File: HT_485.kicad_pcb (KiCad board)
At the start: 2 copper layers, 82 x 72.2 mm, 85 parts, among them J1 POWER, J2 485, J3 PT1000, J4 H/T Sensor, J5 PRG, Q1 BC817, Q2 BC817, Q3 BC817, Q4 BC817, U1 MAX14786EAUD+T, U2 TL082, U3 LM2576D2TR4-3.3G, U4 ESP32-S3-WROOM-1-N16R8, U5 CAT3200TDI-GT3, U6 L7815

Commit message: Rifatto schema 485. Master da rifare
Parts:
- removed C1: 4.7uF, Capacitor_SMD:C_0805_2012Metric
- removed C11, C12: 1uF, Capacitor_SMD:C_0805_2012Metric
- removed C13, C9: 10uF, Capacitor_SMD:C_0805_2012Metric
- removed C14, C15, C2, C20, C4, C8: 100nF, Capacitor_SMD:C_0805_2012Metric
- removed C16: 1nF, Capacitor_SMD:C_0805_2012Metric
- removed C17: 1uF/25V, Capacitor_SMD:C_0805_2012Metric
- removed C18, C19: 100uF/25V, Capacitor_SMD:CP_Elec_6.3x7.7
- removed C3: 1uF/16V, Capacitor_SMD:C_0805_2012Metric
- removed C5: 100uF / 50V, Capacitor_SMD:CP_Elec_8x10.5
- removed C6: 1nF/10V, Capacitor_SMD:C_0805_2012Metric
- removed C7: 1000uF/10V, Capacitor_SMD:CP_Elec_10x10.5
- removed D1: VS-30BQ060HM3/9AT, Diode_SMD:D_SMB-SMC_Universal_Handsoldering
- removed D10: STPS0520Z, Diode_SMD:D_SOD-123
- removed D2: 3.9V/1W, Diode_SMD:D_SMA
- removed D3: PWR, LED_SMD:LED_0805_2012Metric
- removed D4, D5, D6, D7, D8: 1N4148WS, Diode_SMD:D_SOD-323
- removed D9: BAV99, Package_TO_SOT_SMD:SOT-23
- removed J1: POWER, TerminalBlock_Phoenix:TerminalBlock_Phoenix_PT-1,5-2-3.5-H_1x02_P3.50mm_Horizontal
- removed J2: 485, TerminalBlock_Phoenix:TerminalBlock_Phoenix_PT-1,5-2-3.5-H_1x02_P3.50mm_Horizontal
- removed J3: PT1000, TerminalBlock_Phoenix:TerminalBlock_Phoenix_PT-1,5-2-3.5-H_1x02_P3.50mm_Horizontal
- removed J4: H/T Sensor, Connector_JST:JST_PH_S6B-PH-SM4-TB_1x06-1MP_P2.00mm_Horizontal
- removed J5: PRG, Connector_PinSocket_2.54mm:PinSocket_2x03_P2.54mm_Vertical
- removed JP1: BIAS+, Jumper:SolderJumper-2_P1.3mm_Open_RoundedPad1.0x1.5mm
- removed JP2: BIAS-, Jumper:SolderJumper-2_P1.3mm_Open_RoundedPad1.0x1.5mm
- removed JP3: TERMINATOR, Jumper:SolderJumper-2_P1.3mm_Open_RoundedPad1.0x1.5mm
- removed JP4: UART_BOOT_MSG, Jumper:SolderJumper-3_P1.3mm_Bridged12_RoundedPad1.0x1.5mm_NumberLabels
- removed L1: 100uH -MSS1210-104KED, HT485:MSS1210-104KED
- removed Q1, Q2, Q3, Q4: BC817, Package_TO_SOT_SMD:SOT-23
- removed R1, R11, R14, R18, R19, R24, R25, R26, R27, R3, R30, R31, R5, R7, R8: 10K, Resistor_SMD:R_0805_2012Metric_Pad1.20x1.40mm_HandSolder
- removed R10: 100R, Resistor_SMD:R_0805_2012Metric_Pad1.20x1.40mm_HandSolder
- removed R12, R13, R15, R9: 1K, Resistor_SMD:R_0805_2012Metric_Pad1.20x1.40mm_HandSolder
- removed R16, R6: 10R, Resistor_SMD:R_0805_2012Metric_Pad1.20x1.40mm_HandSolder
- removed R17: 3k3, Resistor_SMD:R_0805_2012Metric_Pad1.20x1.40mm_HandSolder
- removed R2: 1K 1%, Resistor_SMD:R_0805_2012Metric_Pad1.20x1.40mm_HandSolder
- removed R20, R21: 370R, Resistor_SMD:R_0805_2012Metric_Pad1.20x1.40mm_HandSolder
- removed R22: 120R, Resistor_SMD:R_0805_2012Metric_Pad1.20x1.40mm_HandSolder
- removed R23: 4K7, Resistor_SMD:R_0805_2012Metric_Pad1.20x1.40mm_HandSolder
- removed R28, R29: 0R, Resistor_SMD:R_0805_2012Metric_Pad1.20x1.40mm_HandSolder
- removed REF** (x4): MountingHole_4.3mm_M4, MountingHole:MountingHole_4.3mm_M4
- removed TP1: D+, TestPoint:TestPoint_Pad_D1.0mm
- removed TP2: D-, TestPoint:TestPoint_Pad_D1.0mm
- removed U1: MAX14786EAUD+T, Package_SO:SOIC-8_3.9x4.9mm_P1.27mm
- removed U2: TL082, Package_SO:SOIC-8-1EP_3.9x4.9mm_P1.27mm_EP2.29x3mm
- removed U3: LM2576D2TR4-3.3G, Package_TO_SOT_SMD:TO-263-5_TabPin3
- removed U4: ESP32-S3-WROOM-1-N16R8, Espressif:ESP32-S3-WROOM-1
- removed U5: CAT3200TDI-GT3, Package_TO_SOT_SMD:TSOT-23-6
- removed U6: L7815, Package_TO_SOT_SMD:TO-263-2
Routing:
- net GND: track 145.7 -> 0.00 mm, vias 3 -> 0
- net +3V3: track 117.3 -> 0.00 mm, vias 6 -> 0
- net +24V: track 79.0 -> 0.00 mm, vias 3 -> 0
- net +5V: track 27.1 -> 0.00 mm, vias 2 -> 0
- net Net-(D1-Pad1): track 25.5 -> 0.00 mm
- net /D+: track 5.73 -> 0.00 mm
- net /D-: track 4.16 -> 0.00 mm
- net Net-(C11-Pad1): track 2.51 -> 0.00 mm
- net Net-(C11-Pad2): track 2.51 -> 0.00 mm
- net Net-(C6-Pad1): track 2.05 -> 0.00 mm
- removed copper zone on F.Cu, net GND
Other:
- board text removed: "${COMPANY} ${TITLE} V: ${REVISION} DATE: ${ISSUE_DATE} ${COMMENT1}"
- board text removed: "+24V DC"
- board text removed: "A"
- board text removed: "B"
- board text removed: "GND"

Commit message: Rivisto tutta la scheda
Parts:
- added C10: 1nF/25V, Capacitor_SMD:C_0805_2012Metric, F.Cu at (94.0, 134.0)
- added C11: 100nF, Capacitor_SMD:C_0805_2012Metric, F.Cu at (137.8, 151.3)
- added C12: 100nF, Capacitor_SMD:C_0805_2012Metric, F.Cu at (150.8, 136.8)
- added C13: 100nF, Capacitor_SMD:C_0805_2012Metric, F.Cu at (138.8, 136.5)
- added C14: 100nF, Capacitor_SMD:C_0805_2012Metric, F.Cu at (143.0, 147.2)
- added C15: 1000uF/25V, Capacitor_SMD:CP_Elec_10x10.5, F.Cu at (112.2, 145.8)
- added C16: 1nF, Capacitor_SMD:C_0805_2012Metric, F.Cu at (121.8, 142.0)
- added C18: 100uF/25V, Capacitor_SMD:CP_Elec_6.3x7.7, F.Cu at (123.5, 158.0)
- added C19: 100uF/25V, Capacitor_SMD:CP_Elec_6.3x7.7, F.Cu at (135.0, 157.5)
- added C20: 100nF, Capacitor_SMD:C_0805_2012Metric, F.Cu at (129.7, 140.2)
- added C21: 1uF / 25V, Capacitor_SMD:C_0805_2012Metric, F.Cu at (116.0, 152.8)
- added C22: 4.7uF, Capacitor_SMD:C_0805_2012Metric, F.Cu at (128.8, 108.0)
- added C23: 4.7uF, Capacitor_SMD:C_0805_2012Metric, F.Cu at (116.5, 108.2)
- added C24: 100nF, Capacitor_SMD:C_0805_2012Metric, F.Cu at (126.5, 108.0)
- added C25: 100nF, Capacitor_SMD:C_0805_2012Metric, F.Cu at (114.2, 108.2)
- added C3: 1uF/16V, Capacitor_SMD:C_0805_2012Metric, F.Cu at (159.9, 106.2)
- added C4: 100nF, Capacitor_SMD:C_0805_2012Metric, F.Cu at (135.2, 141.8)
- added C5: 100uF/75V, Capacitor_SMD:CP_Elec_8x10.5, F.Cu at (95.2, 106.5)
- added C6: 10uF / 25V, Capacitor_SMD:C_0805_2012Metric, F.Cu at (114.2, 135.5)
- added C7: 10uF / 25V, Capacitor_SMD:C_0805_2012Metric, F.Cu at (143.0, 93.8)
- added C8: 100nF, Capacitor_SMD:C_0805_2012Metric, F.Cu at (163.8, 106.2)
- added C9: 10uF, Capacitor_SMD:C_0805_2012Metric, F.Cu at (163.8, 108.5)
- added D1: VS-30BQ060HM3/9AT, Diode_SMD:D_SMB-SMC_Universal_Handsoldering, F.Cu at (101.0, 136.2)
- added D10: BAR43SFILM, Package_TO_SOT_SMD:SOT-23, F.Cu at (125.8, 119.5)
- added D11: BAR43SFILM, Package_TO_SOT_SMD:SOT-23, F.Cu at (125.8, 128.2)
- added D12: BAR43SFILM, Package_TO_SOT_SMD:SOT-23, F.Cu at (125.8, 136.0)
- added D13: BAR43SFILM, Package_TO_SOT_SMD:SOT-23, F.Cu at (137.2, 120.8)
- added D14: BAR43SFILM, Package_TO_SOT_SMD:SOT-23, F.Cu at (137.2, 128.8)
- added D15: VSSAF522-M3/H, Diode_SMD:D_SMA-SMB_Universal_Handsoldering, F.Cu at (103.2, 106.8)
- added D2: BAR43SFILM, Package_TO_SOT_SMD:SOT-23, F.Cu at (113.0, 119.5)
- added D3: PWR, LED_SMD:LED_0805_2012Metric, F.Cu at (110.2, 94.5)
- added D4: 1N4148WS, Diode_SMD:D_SOD-323, F.Cu at (141.5, 151.2)
- added D5: 1N4148WS, Diode_SMD:D_SOD-323, F.Cu at (145.0, 151.2)
- added D6: 1N4148WS, Diode_SMD:D_SOD-323, F.Cu at (119.8, 147.5)
- added D7: 1N4148WS, Diode_SMD:D_SOD-323, F.Cu at (129.5, 156.5)
- added D8: 1N4148WS, Diode_SMD:D_SOD-323, F.Cu at (129.5, 160.0)
- added D9: BAV99, Package_TO_SOT_SMD:SOT-23, F.Cu at (130.8, 147.0)
- added J1: 485_1, TerminalBlock_Phoenix:TerminalBlock_Phoenix_PT-1,5-2-3.5-H_1x02_P3.50mm_Horizontal, F.Cu at (134.2, 96.0)
- added J2: 485_1, TerminalBlock_Phoenix:TerminalBlock_Phoenix_PT-1,5-2-3.5-H_1x02_P3.50mm_Horizontal, F.Cu at (122.0, 96.2)
- added J3: PT1000, TerminalBlock_Phoenix:TerminalBlock_Phoenix_PT-1,5-2-3.5-H_1x02_P3.50mm_Horizontal, F.Cu at (142.2, 158.2)
- added J4: H/T Sensor, Connector_JST:JST_PH_S6B-PH-SM4-TB_1x06-1MP_P2.00mm_Horizontal, F.Cu at (158.2, 158.0)
- added J5: PRG, Connector_PinSocket_2.54mm:PinSocket_2x03_P2.54mm_Vertical, F.Cu at (169.0, 136.5)
- added J6: PWR, TerminalBlock_Phoenix:TerminalBlock_Phoenix_PT-1,5-2-3.5-H_1x02_P3.50mm_Horizontal, F.Cu at (102.5, 96.0)
- added JP1: TERMINATOR, Jumper:SolderJumper-2_P1.3mm_Open_RoundedPad1.0x1.5mm, F.Cu at (130.6, 103.8)
- added JP3: TERMINATOR, Jumper:SolderJumper-2_P1.3mm_Open_RoundedPad1.0x1.5mm, F.Cu at (118.5, 103.8)
- added L1: MSS1210-104KED -100uH, HT485:MSS1210-104KED, F.Cu at (99.2, 146.2)
- added Q1: BC817, Package_TO_SOT_SMD:SOT-23, F.Cu at (125.3, 150.6)
- added Q10: BS170, Package_TO_SOT_SMD:SOT-23, F.Cu at (137.2, 125.2)
- added Q2: BC817, Package_TO_SOT_SMD:SOT-23, F.Cu at (121.5, 150.8)
- added Q3: BC817, Package_TO_SOT_SMD:SOT-23, F.Cu at (152.0, 109.5)
- added Q4: BC817, Package_TO_SOT_SMD:SOT-23, F.Cu at (152.0, 106.0)
- added Q5: BS170, Package_TO_SOT_SMD:SOT-23, F.Cu at (113.0, 116.0)
- added Q6: BS170, Package_TO_SOT_SMD:SOT-23, F.Cu at (125.8, 116.0)
- added Q7: BS170, Package_TO_SOT_SMD:SOT-23, F.Cu at (125.8, 124.8)
- added Q8: BS170, Package_TO_SOT_SMD:SOT-23, F.Cu at (125.8, 132.5)
- added Q9: BS170, Package_TO_SOT_SMD:SOT-23, F.Cu at (137.2, 117.2)
- added R1: 10K, Resistor_SMD:R_0805_2012Metric_Pad1.20x1.40mm_HandSolder, F.Cu at (103.0, 154.0)
- added R10: 100R, Resistor_SMD:R_0805_2012Metric_Pad1.20x1.40mm_HandSolder, F.Cu at (123.0, 145.2)
- added R11: 10K, Resistor_SMD:R_0805_2012Metric_Pad1.20x1.40mm_HandSolder, F.Cu at (118.8, 150.8)
- added R12: 1K 1%, Resistor_SMD:R_0805_2012Metric_Pad1.20x1.40mm_HandSolder, F.Cu at (147.0, 136.8)
- added R13: 10K 1%, Resistor_SMD:R_0805_2012Metric_Pad1.20x1.40mm_HandSolder, F.Cu at (148.0, 139.8)
- added R14: 10K, Resistor_SMD:R_0805_2012Metric_Pad1.20x1.40mm_HandSolder, F.Cu at (141.8, 137.5)
- added R15: 10K 1%, Resistor_SMD:R_0805_2012Metric_Pad1.20x1.40mm_HandSolder, F.Cu at (146.0, 139.8)
- added R16: 10R, Resistor_SMD:R_0805_2012Metric_Pad1.20x1.40mm_HandSolder, F.Cu at (129.5, 151.0)
- added R17: 33K 1%, Resistor_SMD:R_0805_2012Metric_Pad1.20x1.40mm_HandSolder, F.Cu at (138.8, 138.5)
- added R18: 10K 1%, Resistor_SMD:R_0805_2012Metric_Pad1.20x1.40mm_HandSolder, F.Cu at (129.8, 144.2)
- added R19: 10K, Resistor_SMD:R_0805_2012Metric_Pad1.20x1.40mm_HandSolder, F.Cu at (110.2, 96.5)
- added R2: 1K 1%, Resistor_SMD:R_0805_2012Metric_Pad1.20x1.40mm_HandSolder, F.Cu at (137.8, 149.3)
- added R20: 0R, Resistor_SMD:R_0805_2012Metric_Pad1.20x1.40mm_HandSolder, F.Cu at (107.0, 154.0)
- added R21: 10R, Resistor_SMD:R_0805_2012Metric_Pad1.20x1.40mm_HandSolder, F.Cu at (116.0, 120.0)
- added R22: 120R, Resistor_SMD:R_0805_2012Metric_Pad1.20x1.40mm_HandSolder, F.Cu at (122.2, 103.8)
- added R23: 10R, Resistor_SMD:R_0805_2012Metric_Pad1.20x1.40mm_HandSolder, F.Cu at (128.8, 120.0)
- added R24: 10K, Resistor_SMD:R_0805_2012Metric_Pad1.20x1.40mm_HandSolder, F.Cu at (149.0, 105.5)
- added R25: 10K 1%, Resistor_SMD:R_0805_2012Metric_Pad1.20x1.40mm_HandSolder, F.Cu at (129.8, 142.2)
- added R26: 10K, Resistor_SMD:R_0805_2012Metric_Pad1.20x1.40mm_HandSolder, F.Cu at (161.0, 146.8)
- added R27: 10K, Resistor_SMD:R_0805_2012Metric_Pad1.20x1.40mm_HandSolder, F.Cu at (161.0, 148.8)
- added R28: 0R, Resistor_SMD:R_0805_2012Metric_Pad1.20x1.40mm_HandSolder, F.Cu at (156.0, 109.5)
- added R29: 0R, Resistor_SMD:R_0805_2012Metric_Pad1.20x1.40mm_HandSolder, F.Cu at (156.0, 106.0)
- added R3: 1K 1%, Resistor_SMD:R_0805_2012Metric_Pad1.20x1.40mm_HandSolder, F.Cu at (141.2, 153.5)
- added R30: 10K, Resistor_SMD:R_0805_2012Metric_Pad1.20x1.40mm_HandSolder, F.Cu at (145.0, 110.8)
- added R31: 10R, Resistor_SMD:R_0805_2012Metric_Pad1.20x1.40mm_HandSolder, F.Cu at (128.8, 128.5)
- added R32: 4K7, Resistor_SMD:R_0805_2012Metric_Pad1.20x1.40mm_HandSolder, F.Cu at (116.0, 116.0)
- added R33: 4K7, Resistor_SMD:R_0805_2012Metric_Pad1.20x1.40mm_HandSolder, F.Cu at (128.8, 116.0)
- added R34: 4K7, Resistor_SMD:R_0805_2012Metric_Pad1.20x1.40mm_HandSolder, F.Cu at (128.8, 124.5)
- added R35: 4K7, Resistor_SMD:R_0805_2012Metric_Pad1.20x1.40mm_HandSolder, F.Cu at (109.8, 116.2)
- added R36: 4K7, Resistor_SMD:R_0805_2012Metric_Pad1.20x1.40mm_HandSolder, F.Cu at (122.5, 116.2)
- added R37: 4K7, Resistor_SMD:R_0805_2012Metric_Pad1.20x1.40mm_HandSolder, F.Cu at (122.5, 125.0)
- added R38: 10R, Resistor_SMD:R_0805_2012Metric_Pad1.20x1.40mm_HandSolder, F.Cu at (128.8, 136.8)
- added R39: 10R, Resistor_SMD:R_0805_2012Metric_Pad1.20x1.40mm_HandSolder, F.Cu at (140.2, 121.5)
- added R4: 5K6 1%, Resistor_SMD:R_0805_2012Metric_Pad1.20x1.40mm_HandSolder, F.Cu at (143.8, 140.5)
- added R40: 10R, Resistor_SMD:R_0805_2012Metric_Pad1.20x1.40mm_HandSolder, F.Cu at (140.2, 129.5)
- added R41: 4K7, Resistor_SMD:R_0805_2012Metric_Pad1.20x1.40mm_HandSolder, F.Cu at (128.8, 132.8)
- added R42: 4K7, Resistor_SMD:R_0805_2012Metric_Pad1.20x1.40mm_HandSolder, F.Cu at (140.2, 117.5)
- added R43: 4K7, Resistor_SMD:R_0805_2012Metric_Pad1.20x1.40mm_HandSolder, F.Cu at (140.2, 125.5)
- added R44: 4K7, Resistor_SMD:R_0805_2012Metric_Pad1.20x1.40mm_HandSolder, F.Cu at (122.5, 132.8)
- added R45: 4K7, Resistor_SMD:R_0805_2012Metric_Pad1.20x1.40mm_HandSolder, F.Cu at (134.0, 117.5)
- added R46: 4K7, Resistor_SMD:R_0805_2012Metric_Pad1.20x1.40mm_HandSolder, F.Cu at (134.0, 125.5)
- added R47: 120R, Resistor_SMD:R_0805_2012Metric_Pad1.20x1.40mm_HandSolder, F.Cu at (134.3, 103.8)
- added R5: 10K, Resistor_SMD:R_0805_2012Metric_Pad1.20x1.40mm_HandSolder, F.Cu at (119.5, 142.2)
- added R6: 10R, Resistor_SMD:R_0805_2012Metric_Pad1.20x1.40mm_HandSolder, F.Cu at (94.0, 137.8)
- added R7: 10K, Resistor_SMD:R_0805_2012Metric_Pad1.20x1.40mm_HandSolder, F.Cu at (160.0, 108.5)
- added R8: 10K, Resistor_SMD:R_0805_2012Metric_Pad1.20x1.40mm_HandSolder, F.Cu at (149.0, 109.5)
- added R9: 1K, Resistor_SMD:R_0805_2012Metric_Pad1.20x1.40mm_HandSolder, F.Cu at (124.0, 142.2)
- added RV1: 10K 1% 20g -3296Y-1-103LF, Potentiometer_THT:Potentiometer_Bourns_3296Y_Vertical, F.Cu at (152.1, 144.7)
- added SW1: 485_PWR_1, Connector_PinHeader_2.54mm:PinHeader_1x03_P2.54mm_Vertical, F.Cu at (110.8, 104.8)
- added SW2: 485_PWR_2, Connector_PinHeader_2.54mm:PinHeader_1x03_P2.54mm_Vertical, F.Cu at (139.0, 104.9)
- added U1: L7805, Package_TO_SOT_SMD:TO-252-3_TabPin2, F.Cu at (112.8, 128.5)
- added U2: TL082, Package_SO:SOIC-8-1EP_3.9x4.9mm_P1.27mm_EP2.29x3mm, F.Cu at (139.1, 144.0)
- added U3: LD1086DT33TR, Package_TO_SOT_SMD:TO-252-3_TabPin2, F.Cu at (147.8, 97.5)
- added U4: ESP32-S3-WROOM-1U-N16R8, Espressif:ESP32-S3-WROOM-1, F.Cu at (156.0, 122.8)
- added U5: LM2576S-12/NOPB, Package_TO_SOT_SMD:TO-263-5_TabPin3, F.Cu at (99.5, 122.0)
- added U7: TL431DBZ, Package_TO_SOT_SMD:SOT-23, F.Cu at (151.0, 139.8)
- added U8: MAX485, Package_SO:SOIC-8_3.9x4.9mm_P1.27mm, F.Cu at (132.8, 110.0)
- added U9: MAX485, Package_SO:SOIC-8_3.9x4.9mm_P1.27mm, F.Cu at (120.5, 110.0)
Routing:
- net +3V3: track 0.00 -> 462.9 mm, vias 0 -> 89
- net +12V: track 0.00 -> 198.8 mm, vias 0 -> 7
- net GND: track 0.00 -> 197.3 mm, vias 0 -> 22
- net /RTS: track 0.00 -> 106.9 mm, vias 0 -> 9
- net +5V: track 0.00 -> 98.7 mm, vias 0 -> 4
- net /DTR: track 0.00 -> 77.9 mm, vias 0 -> 6
- net /VCC2: track 0.00 -> 69.6 mm, vias 0 -> 5
- net Net-(R1-Pad2): track 0.00 -> 54.8 mm, vias 0 -> 4
- net /PT1000_ADC: track 0.00 -> 54.3 mm, vias 0 -> 2
- net /GPIO0: track 0.00 -> 53.3 mm, vias 0 -> 4
- net /VCC1: track 0.00 -> 48.7 mm, vias 0 -> 4
- net /OP_NEG_V_PWM: track 0.00 -> 47.3 mm, vias 0 -> 2
- net /RX1: track 0.00 -> 34.3 mm, vias 0 -> 2
- net Net-(C11-Pad2): track 0.00 -> 34.0 mm, vias 0 -> 4
- net /RXH2: track 0.00 -> 33.5 mm, vias 0 -> 2
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- added copper zone on B.Cu, net +3V3
- added copper zone on F.Cu, net +3V3
- added copper zone on B.Cu, net GND
- added copper zone on F.Cu, net GND

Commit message: Aggiunto diodo per alimentazione CPU
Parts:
- added D16: 3.9V / 1W, Diode_SMD:D_SOD-128, F.Cu at (169.0, 107.0)
- added REF**: MountingHole_3.2mm_M3, MountingHole:MountingHole_3.2mm_M3, F.Cu at (168.2, 94.8)
- added REF**: MountingHole_3.2mm_M3, MountingHole:MountingHole_3.2mm_M3, F.Cu at (109.5, 159.0)
- added REF**: MountingHole_3.2mm_M3, MountingHole:MountingHole_3.2mm_M3, F.Cu at (93.5, 94.5)
- moved J6 1.00 mm to (103.5, 96.0)
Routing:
- net +24V: track 30.7 -> 22.4 mm, vias 2 -> 20
- net +3V3: track 462.9 -> 467.7 mm, vias 89 -> 76
- net GND: track 197.3 -> 198.4 mm, vias 22 -> 42
- net /VCC2: track 69.6 -> 70.2 mm
- net Net-(D15-Pad2): track 8.16 -> 7.95 mm, vias 0 -> 9
- added copper zone on B.Cu, net +24V
- added copper zone on F.Cu, net +24V
- added copper zone on B.Cu, net Net-(D15-Pad2)
- added copper zone on F.Cu, net Net-(D15-Pad2)

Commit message: Revisionato master
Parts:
- removed REF** (x3): MountingHole_3.2mm_M3, MountingHole:MountingHole_3.2mm_M3
- J6: footprint TerminalBlock_Phoenix:TerminalBlock_Phoenix_PT-1,5-2-3.5-H_1x02_P3.50mm_Horizontal -> TerminalBlock_Phoenix:TerminalBlock_Phoenix_PT-1,5-2-5.0-H_1x02_P5.00mm_Horizontal
- Q10, Q5, Q6, Q7, Q8, Q9: value BS170 -> Si2302CDS
- R12: value 1K 1% -> 560R 1%
- moved R44 18.7 mm to (128.5, 115.0), turned to 180 degrees
- moved D2 12.3 mm to (119.0, 130.2), turned to 90 degrees
- moved R38 12.0 mm to (131.0, 125.0), turned to 180 degrees
- moved Q8 11.9 mm to (131.0, 121.8), turned to 90 degrees
- moved R32 11.4 mm to (119.0, 127.0), turned to 180 degrees
- moved R33 11.1 mm to (127.0, 127.0), turned to 180 degrees
- moved D10 10.8 mm to (127.0, 130.2), turned to 90 degrees
- moved R46 10.6 mm to (132.5, 115.0), turned to 0 degrees
- moved R37 10.2 mm to (120.2, 115.0), turned to 0 degrees
- moved D13 9.66 mm to (139.0, 130.2), turned to 90 degrees
- moved R42 9.58 mm to (139.0, 127.0), turned to 180 degrees
- moved Q5 8.31 mm to (119.0, 121.8), turned to 90 degrees
- moved J5 8.19 mm to (167.3, 144.5)
- moved D12 7.79 mm to (131.0, 130.2), turned to 90 degrees
- moved R40 6.91 mm to (135.0, 125.0), turned to 180 degrees
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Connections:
- net -12V renamed -10V
- Q10 pad 1: /DEH2 -> +3V3
- Q10 pad 2: +3V3 -> Net-(Q10-Pad2)
- Q10 pad 3: Net-(Q10-Pad3) -> /DEH2
- Q5 pad 1: /RXH1 -> +3V3
- Q5 pad 2: +3V3 -> Net-(Q5-Pad2)
- Q5 pad 3: Net-(Q5-Pad3) -> /RXH1
- Q6 pad 1: /TXH1 -> +3V3
- Q6 pad 2: +3V3 -> Net-(Q6-Pad2)
- Q6 pad 3: Net-(Q6-Pad3) -> /TXH1
- Q7 pad 1: /DEH1 -> +3V3
- Q7 pad 2: +3V3 -> Net-(Q7-Pad2)
- Q7 pad 3: Net-(Q7-Pad3) -> /DEH1
- Q8 pad 1: /RXH2 -> +3V3
- Q8 pad 2: +3V3 -> Net-(Q8-Pad2)
- Q8 pad 3: Net-(Q8-Pad3) -> /RXH2
- Q9 pad 1: /TXH2 -> +3V3
- Q9 pad 2: +3V3 -> Net-(Q9-Pad2)
- Q9 pad 3: Net-(Q9-Pad3) -> /TXH2
- R21 pad 1: Net-(Q5-Pad3) -> Net-(Q5-Pad2)
- R23 pad 1: Net-(Q6-Pad3) -> Net-(Q6-Pad2)
- R31 pad 1: Net-(Q7-Pad3) -> Net-(Q7-Pad2)
- R32 pad 1: Net-(Q5-Pad3) -> Net-(Q5-Pad2)
- R33 pad 1: Net-(Q6-Pad3) -> Net-(Q6-Pad2)
- R34 pad 1: Net-(Q7-Pad3) -> Net-(Q7-Pad2)
- R38 pad 1: Net-(Q8-Pad3) -> Net-(Q8-Pad2)
- R39 pad 1: Net-(Q9-Pad3) -> Net-(Q9-Pad2)
- R40 pad 1: Net-(Q10-Pad3) -> Net-(Q10-Pad2)
- R41 pad 1: Net-(Q8-Pad3) -> Net-(Q8-Pad2)
- R42 pad 1: Net-(Q9-Pad3) -> Net-(Q9-Pad2)
- R43 pad 1: Net-(Q10-Pad3) -> Net-(Q10-Pad2)
- U4 pad 15: /TX1 -> /RX1
- U4 pad 17: /RX1 -> /DE1
- U4 pad 18: /DE1 -> /TX1
- U4 pad 20: /TX2 -> /RX2
- U4 pad 22: /RX2 -> /TX2
- U4 pad 33: /SDA -> /SCL
- U4 pad 34: /SCL -> /SDA
- U4 pad 35: /ALERT -> /RESET
- U4 pad 38: /RESET -> /ALERT
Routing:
- net +3V3: track 467.7 -> 337.5 mm
- net GND: track 198.4 -> 236.5 mm, vias 42 -> 31
- net /VCC2: track 70.2 -> 37.9 mm, vias 5 -> 4
- net /RXH2: track 33.5 -> 9.58 mm, vias 2 -> 0
- net /VCC1: track 48.7 -> 28.8 mm
- net Net-(R4-Pad1): track 29.1 -> 10.6 mm, vias 3 -> 1
- net /RTS: track 106.7 -> 95.2 mm, vias 9 -> 8
- net /ALERT: track 32.6 -> 23.8 mm, vias 4 -> 0
- net /RX1: track 34.3 -> 42.1 mm, vias 2 -> 4
- net /RESET: track 31.8 -> 24.8 mm, vias 4 -> 0
- net /TX1: track 24.5 -> 31.4 mm, vias 2 -> 4
- net /DE1: track 29.4 -> 36.2 mm, vias 2 -> 4
- net Net-(Q5-Pad3): track 6.62 -> 0.00 mm
- net /DEH1: track 18.9 -> 12.3 mm, vias 2 -> 0
- net /RX2: track 31.4 -> 24.8 mm, vias 2 -> 4
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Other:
- board text added: "+24VDC"
- board text added: "A"
- board text added: "A B"
- board text added: "B"
- board text added: "GND"

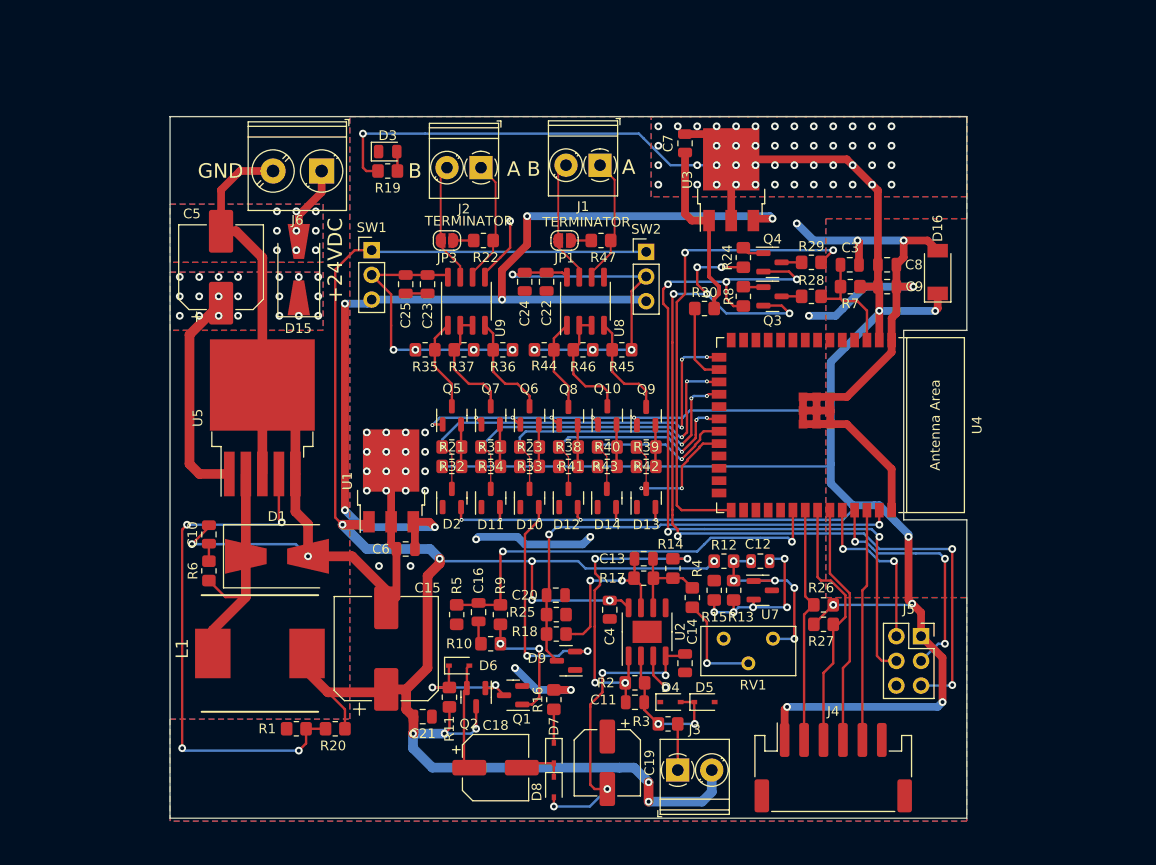
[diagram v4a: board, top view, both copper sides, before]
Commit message: Aggiunti logo MME. Versione 1.0.1.0
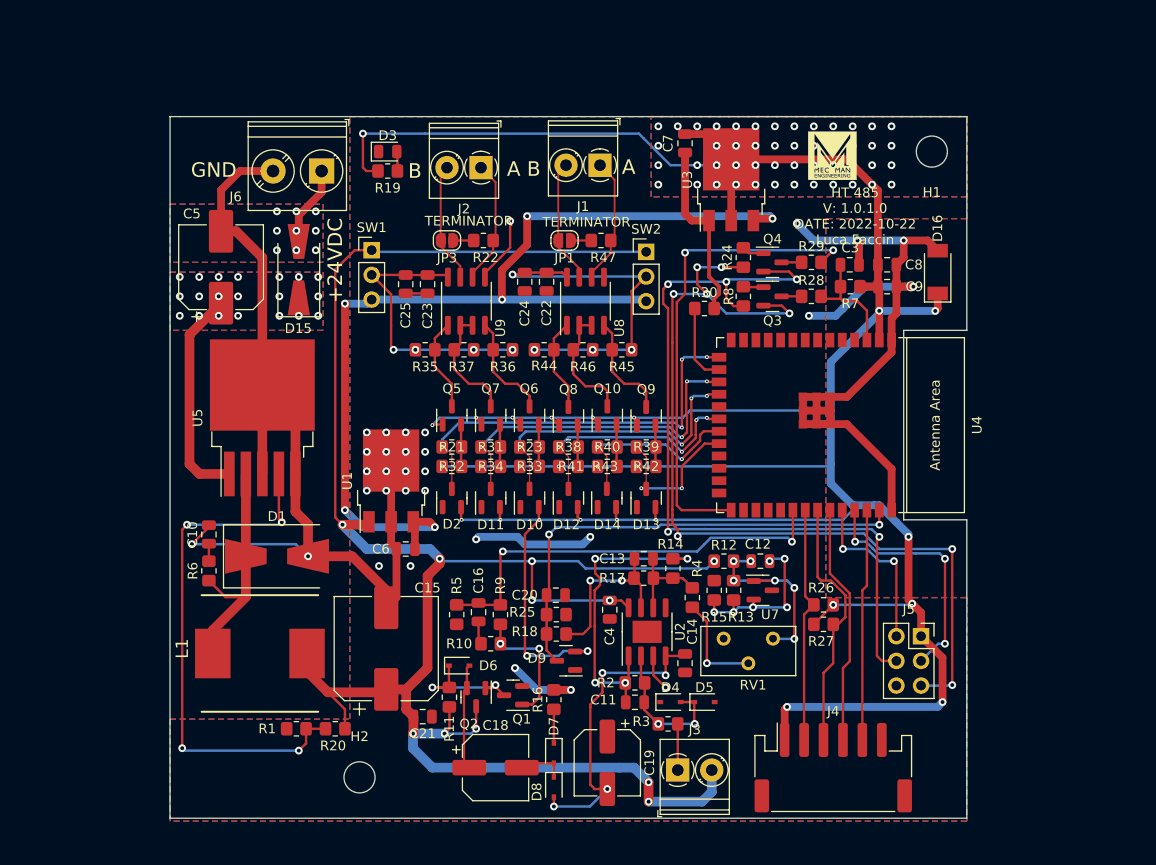
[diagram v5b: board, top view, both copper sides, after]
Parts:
- added H1: MountingHole, MountingHole:MountingHole_3.2mm_M3, F.Cu at (168.4, 94.6)
- added H2: MountingHole, MountingHole:MountingHole_3.2mm_M3, F.Cu at (109.5, 159.0)
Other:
- board text added: "${TITLE} V: ${REVISION} DATE: ${ISSUE_DATE} ${COMMENT1}"

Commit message: Messi connettori 485 a passo 5. Aggiornata versione a 1.0.1.1
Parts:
- J1, J2: footprint TerminalBlock_Phoenix:TerminalBlock_Phoenix_PT-1,5-2-3.5-H_1x02_P3.50mm_Horizontal -> TerminalBlock_Phoenix:TerminalBlock_Phoenix_PT-1,5-2-5.0-H_1x02_P5.00mm_Horizontal
- JP1: value TERMINATOR -> T
- JP3: value TERMINATOR -> T.
- moved J1 0.75 mm to (134.9, 96.4)
- moved J2 0.60 mm to (122.6, 96.4)
